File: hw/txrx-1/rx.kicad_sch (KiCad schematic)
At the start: 32 parts, among them U1 SN74CBT3253, U2 LM4562, U3 LM4562

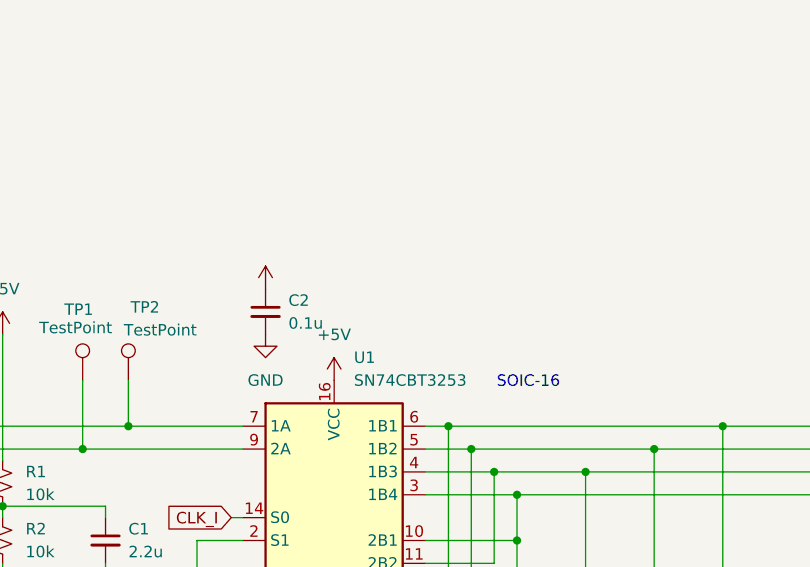
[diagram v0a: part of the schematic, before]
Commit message: Initial PCB layout for TXRX board
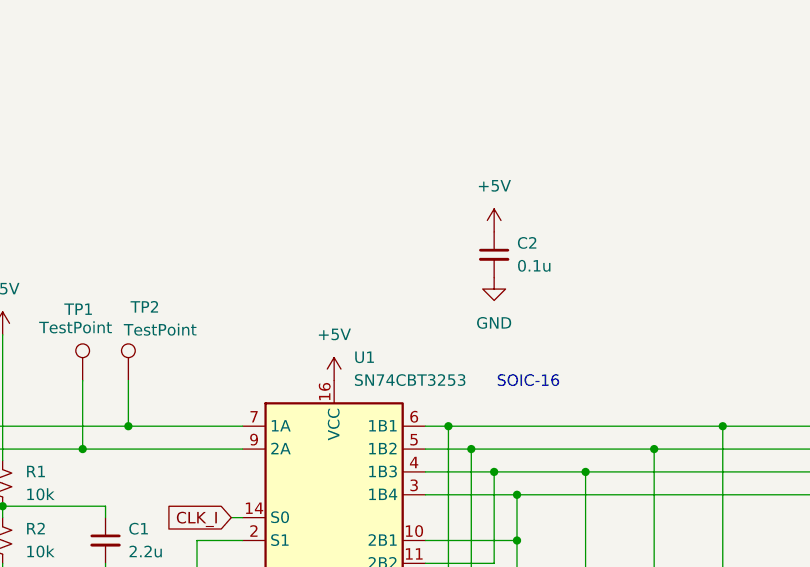
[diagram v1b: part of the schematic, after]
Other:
- company: (none) -> Bruce MacKinnon KC1FSZ
- title: (none) -> Quadrature TX/RX Board
- moved on the sheet: C2
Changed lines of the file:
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@@
 	(generator "eeschema")
 	(generator_version "8.0")
-	(paper "A4")
+	(paper "USLetter")
+	(title_block
+		(title "Quadrature TX/RX Board")
+		(date "2025-02-16")
+		(rev "1")
+		(company "Bruce MacKinnon KC1FSZ")
+		(comment 1 "Copyright (C) Bruce MacKinnon, 2025")
+		(comment 2 "NOT FOR COMMERCIAL USE")
+	)
 	(junction
 		(at 63.5 82.55)
@@
 	)
 	(symbol
-		(lib_id "power:+5V")
-		(at 83.82 64.77 0)
-		(unit 1)
-		(exclude_from_sim no)
-		(in_bom yes)
-		(on_board yes)
-		(dnp no)
-		(property "Reference" "#PWR06"
-			(at 83.82 68.58 0)
-			(effects
-				(font
-					(size 1.27 1.27)
-				)
-				(hide yes)
-			)
-		)
-		(property "Value" "+5V"
-			(at 83.82 54.61 0)
-			(effects
-				(font
-					(size 1.27 1.27)
-				)
-				(hide yes)
-			)
-		)
-		(property "Footprint" ""
-			(at 83.82 64.77 0)
-			(effects
-				(font
-					(size 1.27 1.27)
-				)
-				(hide yes)
-			)
-		)
-		(property "Datasheet" ""
-			(at 83.82 64.77 0)
-			(effects
-				(font
-					(size 1.27 1.27)
-				)
-				(hide yes)
-			)
-		)
-		(property "Description" "Power symbol creates a global label with name \"+5V\""
-			(at 83.82 64.77 0)
-			(effects
-				(font
-					(size 1.27 1.27)
-				)
-				(hide yes)
-			)
-		)
-		(pin "1"
-		)
-		(instances
-			(project "txrx-1"
-				(path "/8e82f983-38e6-4304-be32-fb6d88cc8acc/18a6c186-38de-4d45-956c-bdfe41b0c978"
-					(reference "#PWR06")
-					(unit 1)
-				)
-			)
-		)
-	)
-	(symbol
 		(lib_id "power:GND")
 		(at 127 119.38 0)
@@
 	)
 	(symbol
+		(lib_id "power:+5V")
+		(at 109.22 58.42 0)
+		(unit 1)
+		(exclude_from_sim no)
+		(in_bom yes)
+		(on_board yes)
+		(dnp no)
+		(fields_autoplaced yes)
+		(property "Reference" "#PWR06"
+			(at 109.22 62.23 0)
+			(effects
+				(font
+					(size 1.27 1.27)
+				)
+				(hide yes)
+			)
+		)
+		(property "Value" "+5V"
+			(at 109.22 53.34 0)
+			(effects
+				(font
+					(size 1.27 1.27)
+				)
+			)
+		)
+		(property "Footprint" ""
+			(at 109.22 58.42 0)
+			(effects
+				(font
+					(size 1.27 1.27)
+				)
+				(hide yes)
+			)
+		)
+		(property "Datasheet" ""
+			(at 109.22 58.42 0)
+			(effects
+				(font
+					(size 1.27 1.27)
+				)
+				(hide yes)
+			)
+		)
+		(property "Description" "Power symbol creates a global label with name \"+5V\""
+			(at 109.22 58.42 0)
+			(effects
+				(font
+					(size 1.27 1.27)
+				)
+				(hide yes)
+			)
+		)
+		(pin "1"
+		)
+		(instances
+			(project ""
+				(path "/8e82f983-38e6-4304-be32-fb6d88cc8acc/18a6c186-38de-4d45-956c-bdfe41b0c978"
+					(reference "#PWR06")
+					(unit 1)
+				)
+			)
+		)
+	)
+	(symbol
 		(lib_id "Device:R_Small_US")
 		(at 210.82 114.3 0)
@@
 	(symbol
 		(lib_id "Device:C_Small")
-		(at 83.82 67.31 0)
+		(at 109.22 60.96 0)
 		(unit 1)
 		(exclude_from_sim no)
@@
 		(fields_autoplaced yes)
 		(property "Reference" "C2"
-			(at 86.36 66.0462 0)
+			(at 111.76 59.6962 0)
 			(effects
 				(font
@@
 		)
 		(property "Value" "0.1u"
-			(at 86.36 68.5862 0)
+			(at 111.76 62.2362 0)
 			(effects
 				(font
@@
 		)
 		(property "Footprint" "Capacitor_SMD:C_0805_2012Metric_Pad1.18x1.45mm_HandSolder"
-			(at 83.82 67.31 0)
+			(at 109.22 60.96 0)
 			(effects
 				(font
@@
 		)
 		(property "Datasheet" "~"
-			(at 83.82 67.31 0)
+			(at 109.22 60.96 0)
 			(effects
 				(font
@@
 		)
 		(property "Description" "Unpolarized capacitor, small symbol"
-			(at 83.82 67.31 0)
+			(at 109.22 60.96 0)
 			(effects
 				(font
@@
 	(symbol
 		(lib_id "power:GND")
-		(at 83.82 69.85 0)
+		(at 109.22 63.5 0)
 		(unit 1)
 		(exclude_from_sim no)
@@
 		(fields_autoplaced yes)
 		(property "Reference" "#PWR07"
-			(at 83.82 76.2 0)
+			(at 109.22 69.85 0)
 			(effects
 				(font
@@
 		)
 		(property "Value" "GND"
-			(at 83.82 74.93 0)
+			(at 109.22 68.58 0)
 			(effects
 				(font
@@
 		)
 		(property "Footprint" ""
-			(at 83.82 69.85 0)
+			(at 109.22 63.5 0)
 			(effects
 				(font
@@
 		)
 		(property "Datasheet" ""
-			(at 83.82 69.85 0)
+			(at 109.22 63.5 0)
 			(effects
 				(font
@@
 		)
 		(property "Description" "Power symbol creates a global label with name \"GND\" , ground"
-			(at 83.82 69.85 0)
+			(at 109.22 63.5 0)
 			(effects
 				(font
